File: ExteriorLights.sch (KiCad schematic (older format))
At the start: 28 parts, among them J1 Left_Signal, J2 Right_Signal, J3 Brake Light, J4 Headlight, U1 EL3H7, U2 EL3H7, U3 EL3H7, U4 EL3H7

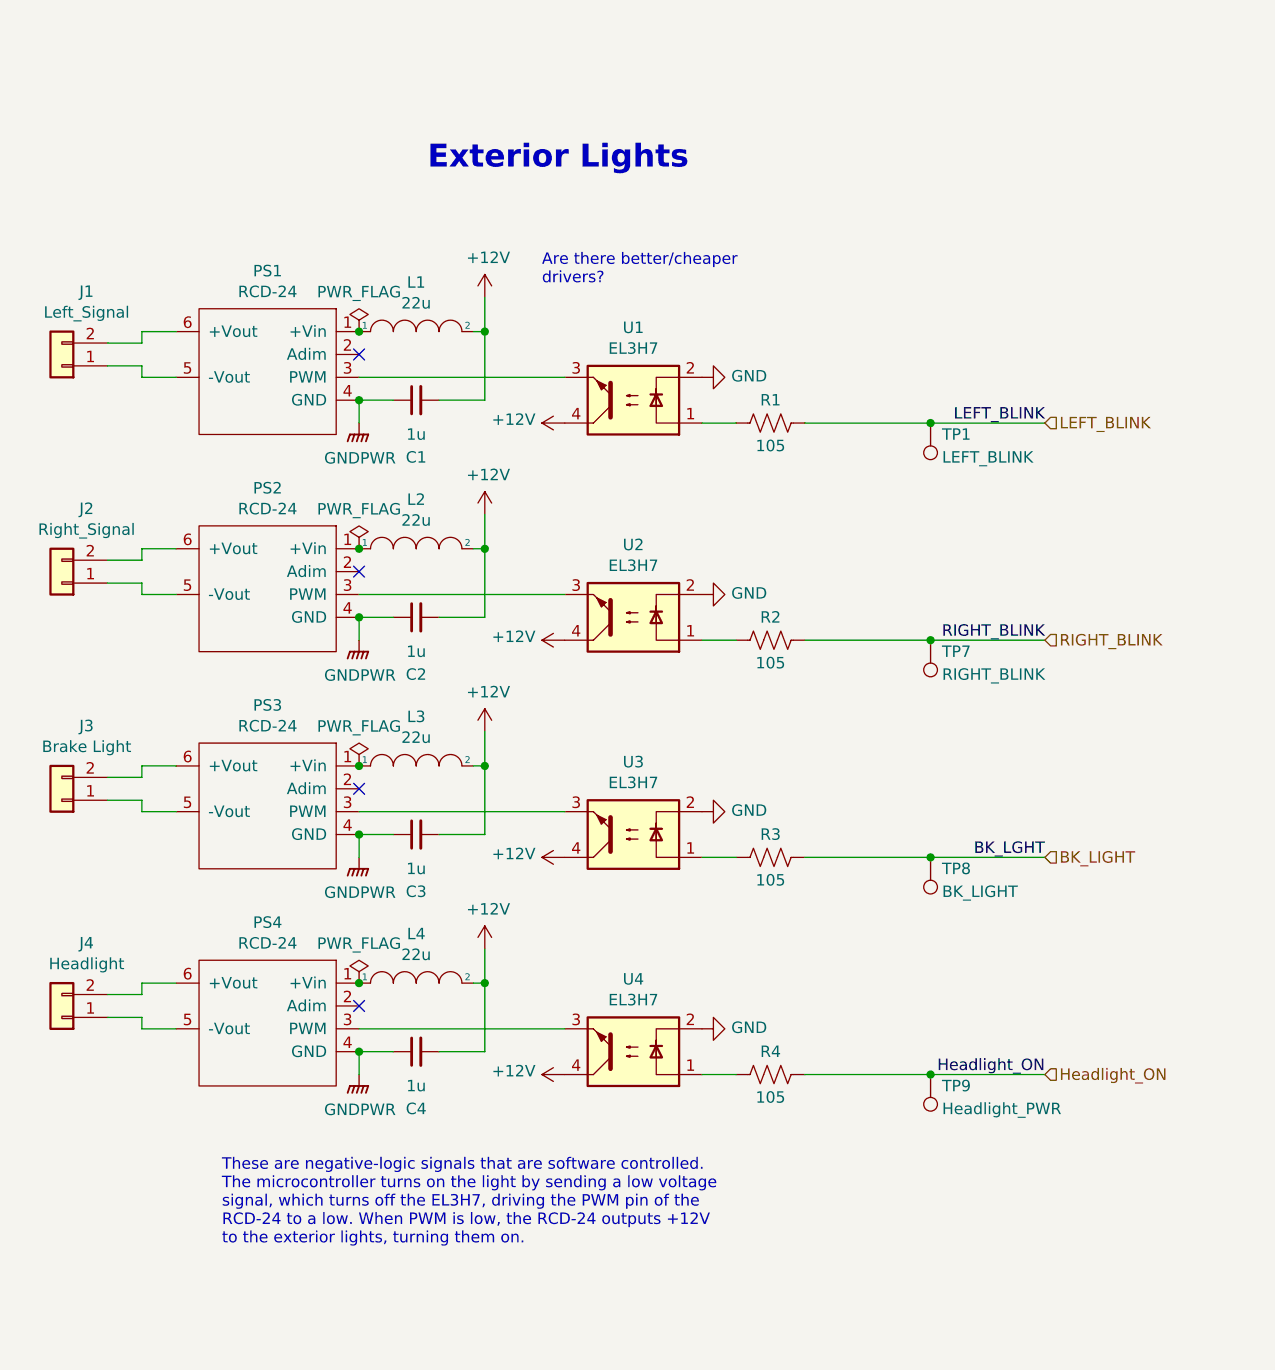
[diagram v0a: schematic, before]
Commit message: Adds backup camera
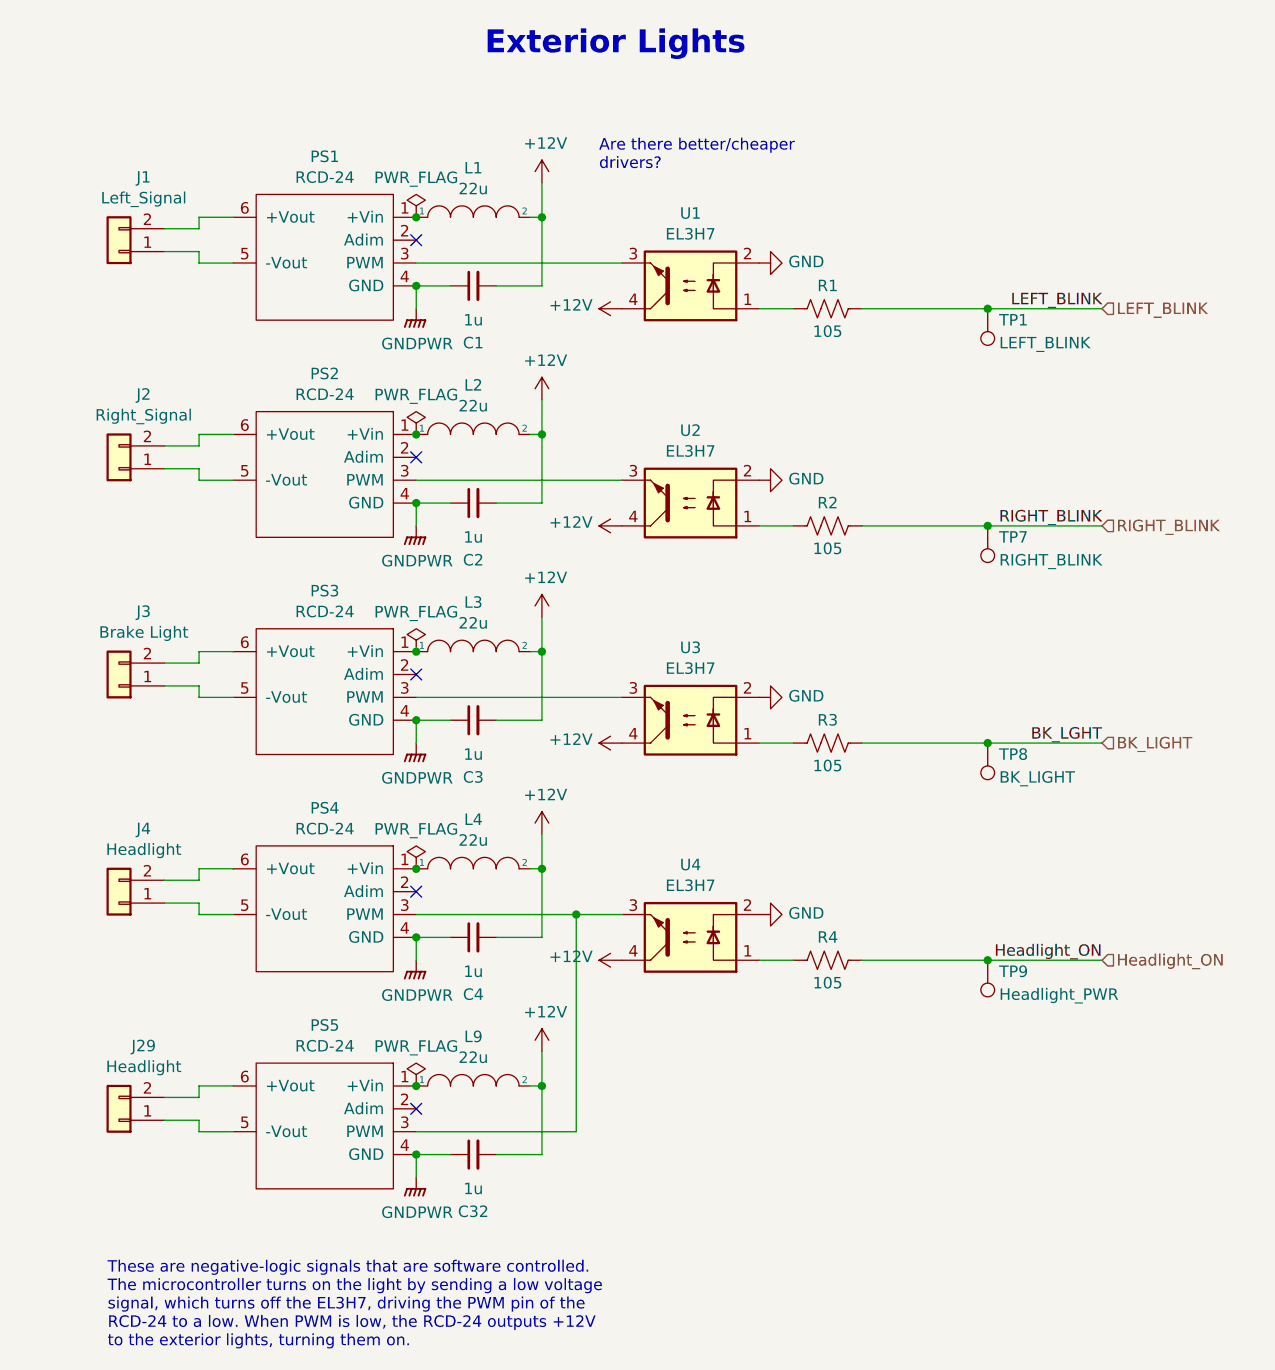
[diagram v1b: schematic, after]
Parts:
- added C32: 1u, Capacitor_SMD:C_0805_2012Metric, symbol Device:C_Small
- added J29: Headlight, UTSVT_Connectors:Molex_MicroFit3.0_1x2xP3.00mm_PolarizingPeg_Vertical, symbol Connector_Generic:Conn_01x02
- added L9: 22u, Inductor_SMD:L_0805_2012Metric, symbol pspice:INDUCTOR
- added PS5: RCD-24, UTSVT_Special:RCD-24, symbol Dash:RCD-24
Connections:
- net +12V: now also C32.2, L9.2
- net GNDPWR: now also C32.1, PS5.4 (GND)
- net at PS4.3 (PWM), U4.3: now also PS5.3 (PWM)
- new net: J29.1 (Pin_1), PS5.5 (-Vout)
- new net: J29.2 (Pin_2), PS5.6 (+Vout)
- new net: L9.1, PS5.1 (+Vin)
- no-connect marks 4 -> 5
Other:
- moved on the sheet: C1, C2, C3, C4, J1, J2, J3, J4, L1, L2, L3, L4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
